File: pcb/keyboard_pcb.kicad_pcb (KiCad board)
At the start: 2 copper layers, 138.8 x 89.9 mm, 23 parts, among them J1 TRRS, K00 KEYSW, K01 KEYSW, K02 KEYSW, K03 KEYSW, K04 KEYSW, K05 KEYSW, K10 KEYSW, K11 KEYSW, K12 KEYSW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

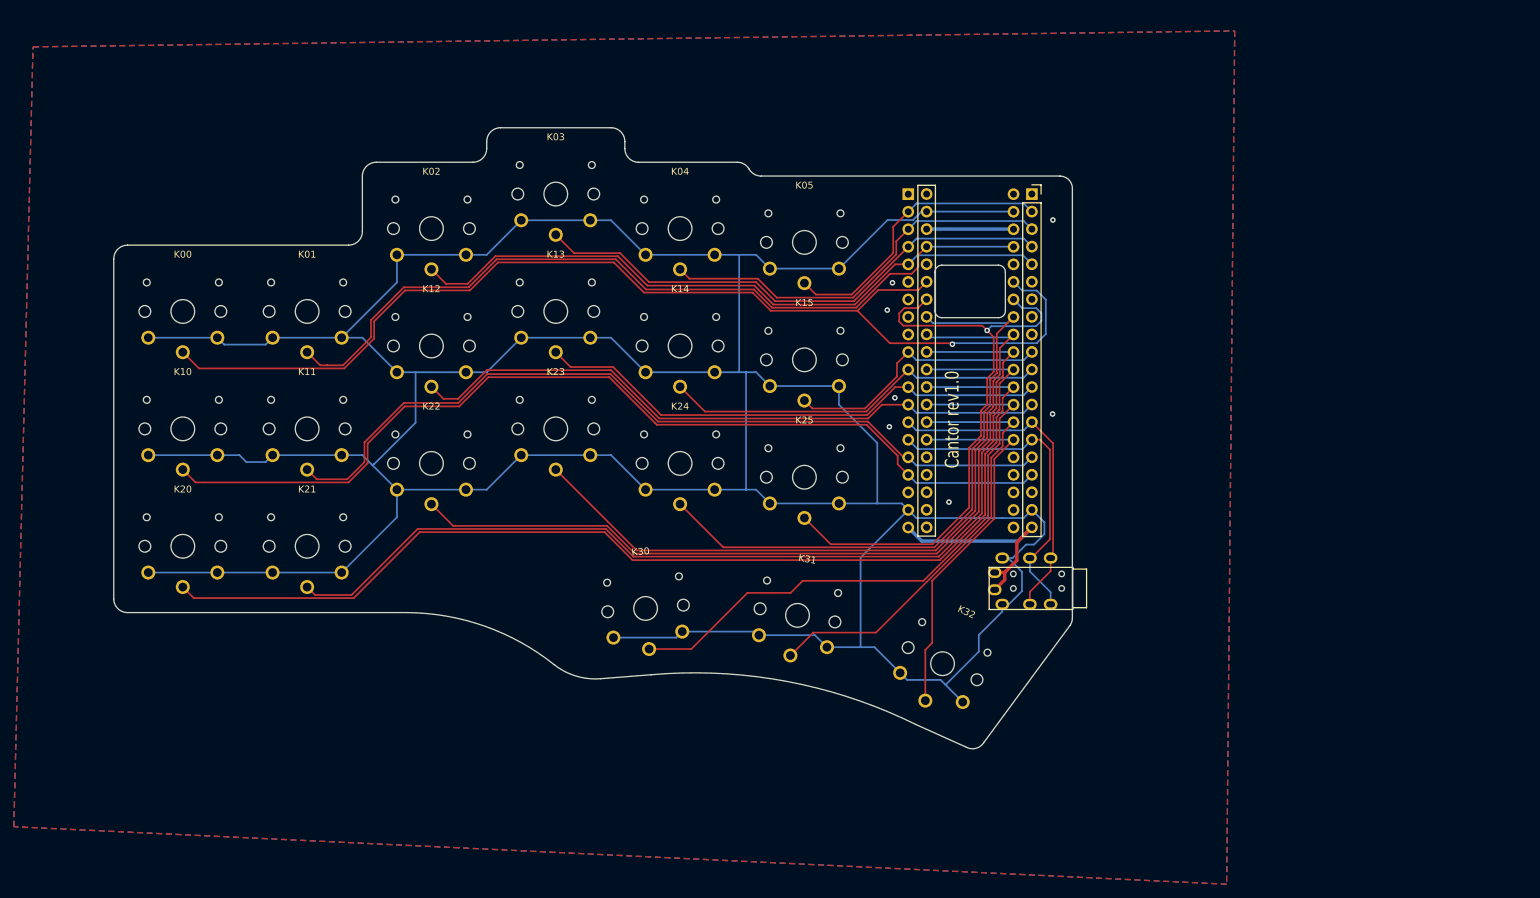
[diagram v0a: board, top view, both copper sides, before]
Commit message: WIP: adding  RP2040 + oled
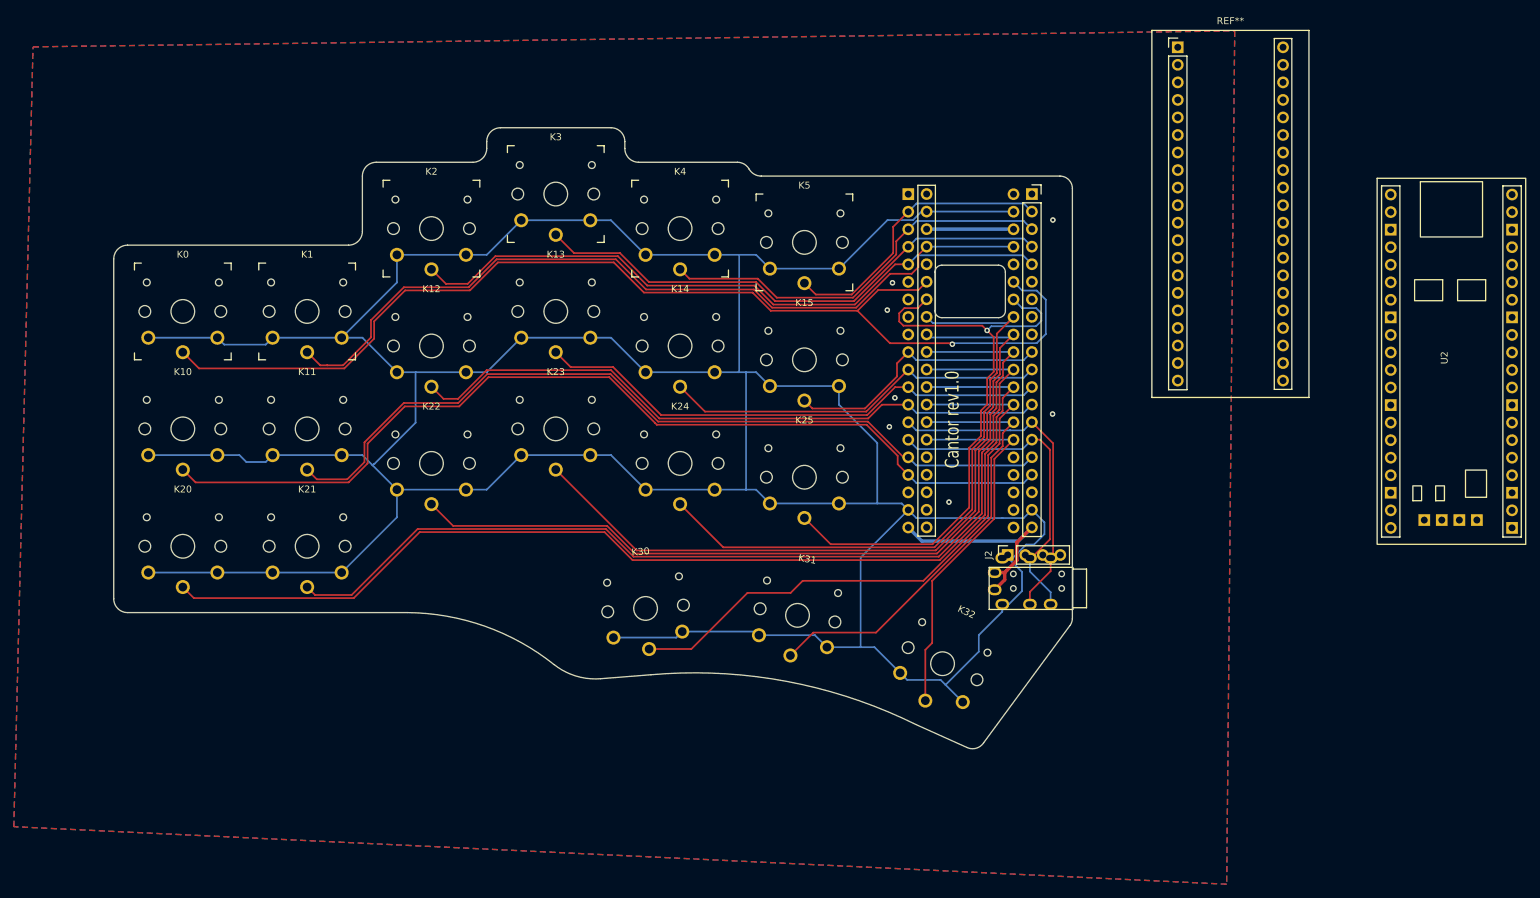
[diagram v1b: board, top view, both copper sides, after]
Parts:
- removed K00, K01, K02, K03, K04, K05: KEYSW, keyswitches:SW_PG1350_reversible
- added J2: Conn_01x04_Female, Connector_PinSocket_2.54mm:PinSocket_1x04_P2.54mm_Vertical, F.Cu at (193.4, 105.3)
- added K0: KEYSW, keyswitches:SW_PG1350_reversible, F.Cu at (74.0, 70.0)
- added K1: KEYSW, keyswitches:SW_PG1350_reversible, F.Cu at (92.0, 70.0)
- added K2: KEYSW, keyswitches:SW_PG1350_reversible, F.Cu at (110.0, 58.0)
- added K3: KEYSW, keyswitches:SW_PG1350_reversible, F.Cu at (128.0, 53.0)
- added K4: KEYSW, keyswitches:SW_PG1350_reversible, F.Cu at (146.0, 58.0)
- added K5: KEYSW, keyswitches:SW_PG1350_reversible, F.Cu at (164.0, 60.0)
- added REF**: WeAct BlackPill, Footprints:YAAJ_WeAct_BlackPill_2, F.Cu at (218.1, 31.8)
- added U2: WeAct-RP2040-Pico, rp2040:WeAct-RP2040-Pico, F.Cu at (257.7, 77.2)
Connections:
- U1 pad 10: /k15 -> unconnected-(U1-Pad10)
- U1 pad 11: /k14 -> unconnected-(U1-Pad11)
- U1 pad 12: /k13 -> unconnected-(U1-Pad12)
- U1 pad 13: /k12 -> unconnected-(U1-Pad13)
- U1 pad 14: /TX -> unconnected-(U1-Pad14)
- U1 pad 15: /RX -> unconnected-(U1-Pad15)
- U1 pad 16: /k11 -> unconnected-(U1-Pad16)
- U1 pad 17: /k10 -> unconnected-(U1-Pad17)
- U1 pad 19: GND -> unconnected-(U1-Pad19)
- U1 pad 2: /k05 -> unconnected-(U1-Pad2)
- U1 pad 20: +3V3 -> unconnected-(U1-Pad20)
- U1 pad 26: /k32 -> unconnected-(U1-Pad26)
- U1 pad 27: /k31 -> unconnected-(U1-Pad27)
- U1 pad 28: /k30 -> unconnected-(U1-Pad28)
- U1 pad 29: /k20 -> unconnected-(U1-Pad29)
- U1 pad 3: /k04 -> unconnected-(U1-Pad3)
- U1 pad 30: /k21 -> unconnected-(U1-Pad30)
- U1 pad 31: /k22 -> unconnected-(U1-Pad31)
- U1 pad 32: /k23 -> unconnected-(U1-Pad32)
- U1 pad 33: /k24 -> unconnected-(U1-Pad33)
- U1 pad 34: /k25 -> unconnected-(U1-Pad34)
- U1 pad 35: /k00 -> unconnected-(U1-Pad35)
- U1 pad 37: /k01 -> unconnected-(U1-Pad37)
- U1 pad 38: +3V3 -> unconnected-(U1-Pad38)
- U1 pad 39: GND -> unconnected-(U1-Pad39)
- U1 pad 4: /k03 -> unconnected-(U1-Pad4)
- U1 pad 5: /k02 -> unconnected-(U1-Pad5)
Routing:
- net unconnected-(U1-Pad35): track 0.00 -> 161.7 mm, vias 0 -> 1
- net /k00: track 161.7 -> 0.00 mm, vias 1 -> 0
- net unconnected-(U1-Pad29): track 0.00 -> 157.9 mm
- net /k20: track 157.9 -> 0.00 mm
- net unconnected-(U1-Pad30): track 0.00 -> 141.7 mm
- net /k21: track 141.7 -> 0.00 mm
- net unconnected-(U1-Pad17): track 0.00 -> 139.2 mm
- net /k10: track 139.2 -> 0.00 mm
- net unconnected-(U1-Pad31): track 0.00 -> 122.5 mm
- net /k22: track 122.5 -> 0.00 mm
- net unconnected-(U1-Pad16): track 0.00 -> 119.5 mm
- net /k11: track 119.5 -> 0.00 mm
- net unconnected-(U1-Pad37): track 0.00 -> 118.5 mm
- net /k01: track 118.5 -> 0.00 mm
- net unconnected-(U1-Pad32): track 0.00 -> 108.7 mm
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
